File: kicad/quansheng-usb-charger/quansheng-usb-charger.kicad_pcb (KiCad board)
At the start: 2 copper layers, 43 x 47.5 mm, 30 parts, among them J1 USB_C_Receptacle_USB2.0, U1 IP2326

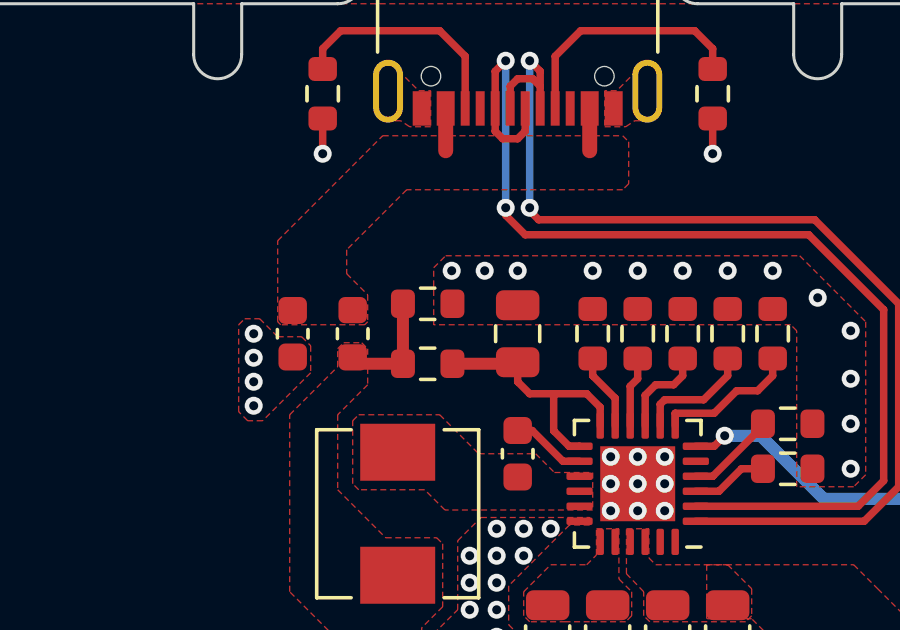
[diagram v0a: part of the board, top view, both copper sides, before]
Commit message: Add JLCPCB files and README
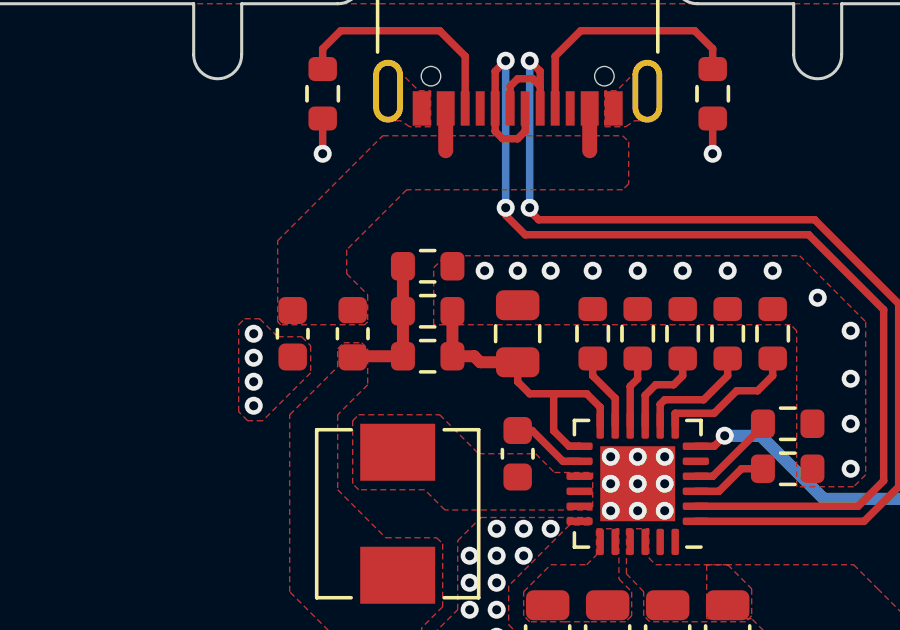
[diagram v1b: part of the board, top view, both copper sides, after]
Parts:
- removed REF**: OSHW-Logo2_36.5x30mm_SilkScreen, Symbol:OSHW-Logo2_36.5x30mm_SilkScreen
- added R13: 1R, Resistor_SMD:R_0603_1608Metric, F.Cu at (116.0, 95.2)
- FB1: value BLM18PG121SN1D -> BLM18KG121TN1D
- R6: value 0.47R -> 1R
- moved R3 1.25 mm to (116.0, 93.8)
- moved R6 0.25 mm to (116.0, 96.8)
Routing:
- net Net-(C2-Pad1): track 8.87 -> 10.4 mm
- net /VBUS: track 43.6 -> 44.9 mm

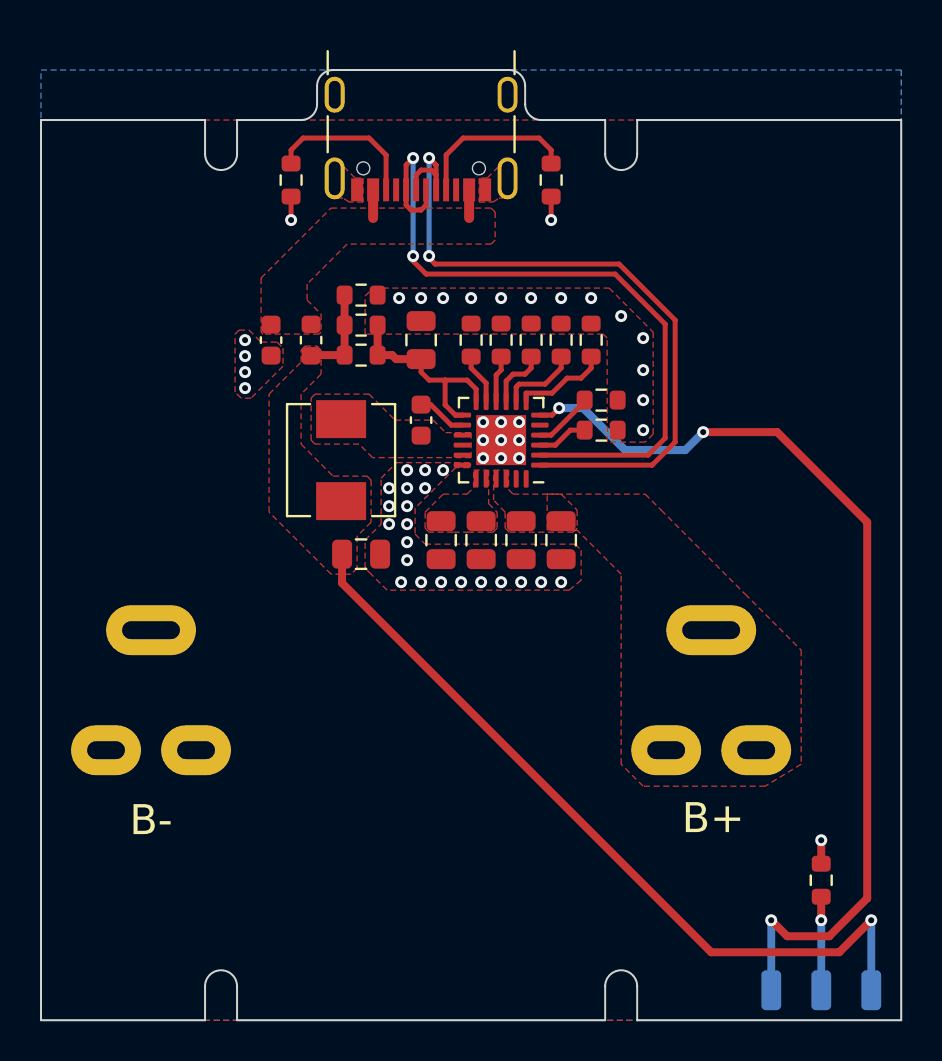
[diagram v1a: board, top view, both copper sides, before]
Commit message: Improve mechanical fit
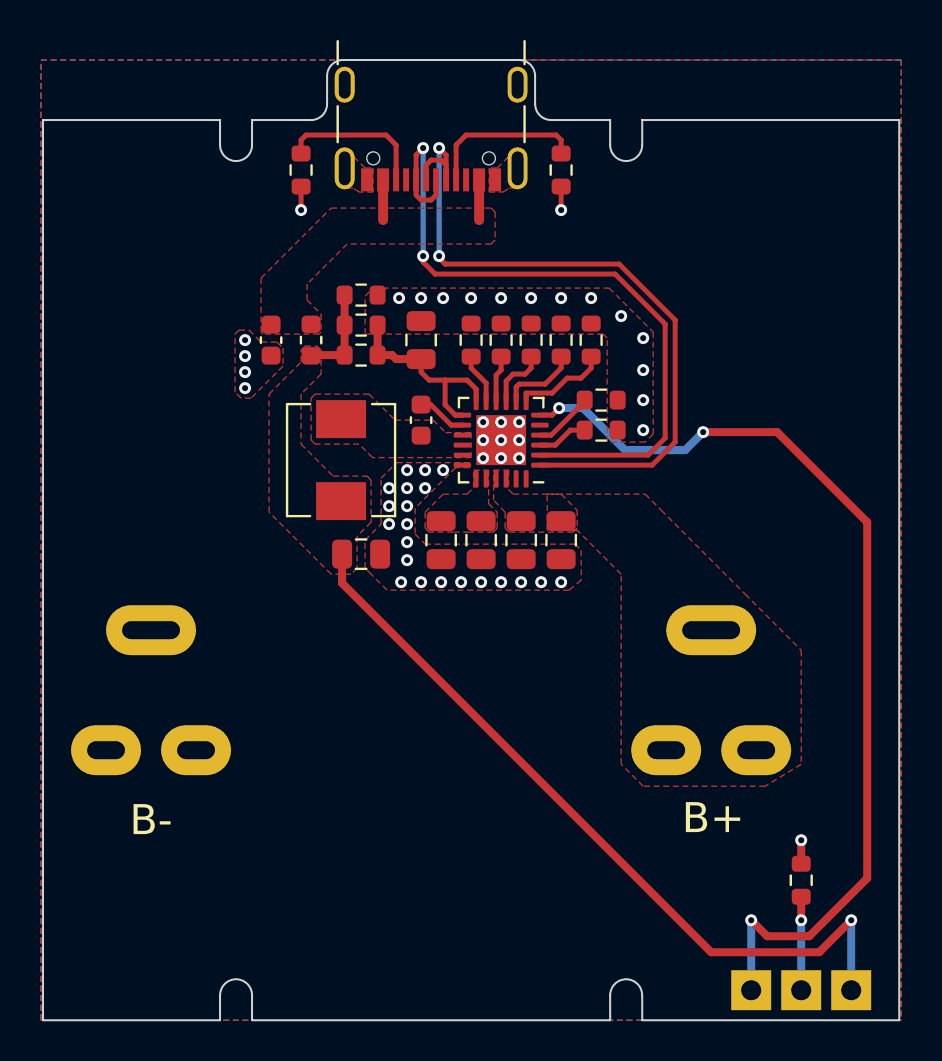
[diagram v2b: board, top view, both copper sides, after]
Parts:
- added REF**: KiCad-Logo_6mm_SilkScreen, Symbol:KiCad-Logo_6mm_SilkScreen, B.Cu at (104.0, 93.5)
- added REF**: OSHW-Logo_19x20mm_SilkScreen, Symbol:OSHW-Logo_19x20mm_SilkScreen, B.Cu at (119.5, 118.5)
- TP3, TP4, TP5: footprint Connector_Wire:SolderWirePad_1x01_SMD_1x2mm -> TestPoint:TestPoint_THTPad_2.0x2.0mm_Drill1.0mm
- moved R5 1.00 mm to (138.0, 123.0)
- moved TP3 1.00 mm to (140.5, 128.5)
- moved TP4 1.00 mm to (138.0, 128.5)
- moved TP5 1.00 mm to (135.5, 128.5)
- moved J1 0.71 mm to (119.5, 85.6)
- moved R1 0.71 mm to (113.0, 87.5)
- moved R2 0.71 mm to (126.0, 87.5)
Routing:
- net /VUSB: track 2.82 -> 4.02 mm
- net /VBUS: track 44.9 -> 43.9 mm
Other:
- board size 43 x 47.5 mm -> 42.8 x 48 mm
- board text added: "C"
- board text added: "G"
- board text added: "R"
